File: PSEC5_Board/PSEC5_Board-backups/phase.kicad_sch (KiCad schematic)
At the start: 23 parts, among them U1 MC100LVEL40DWG, U4 OPA607QDBVRQ1, U7 AD4008BCPZ-RL7, Y1 ASE2-40.000MHZ-ET

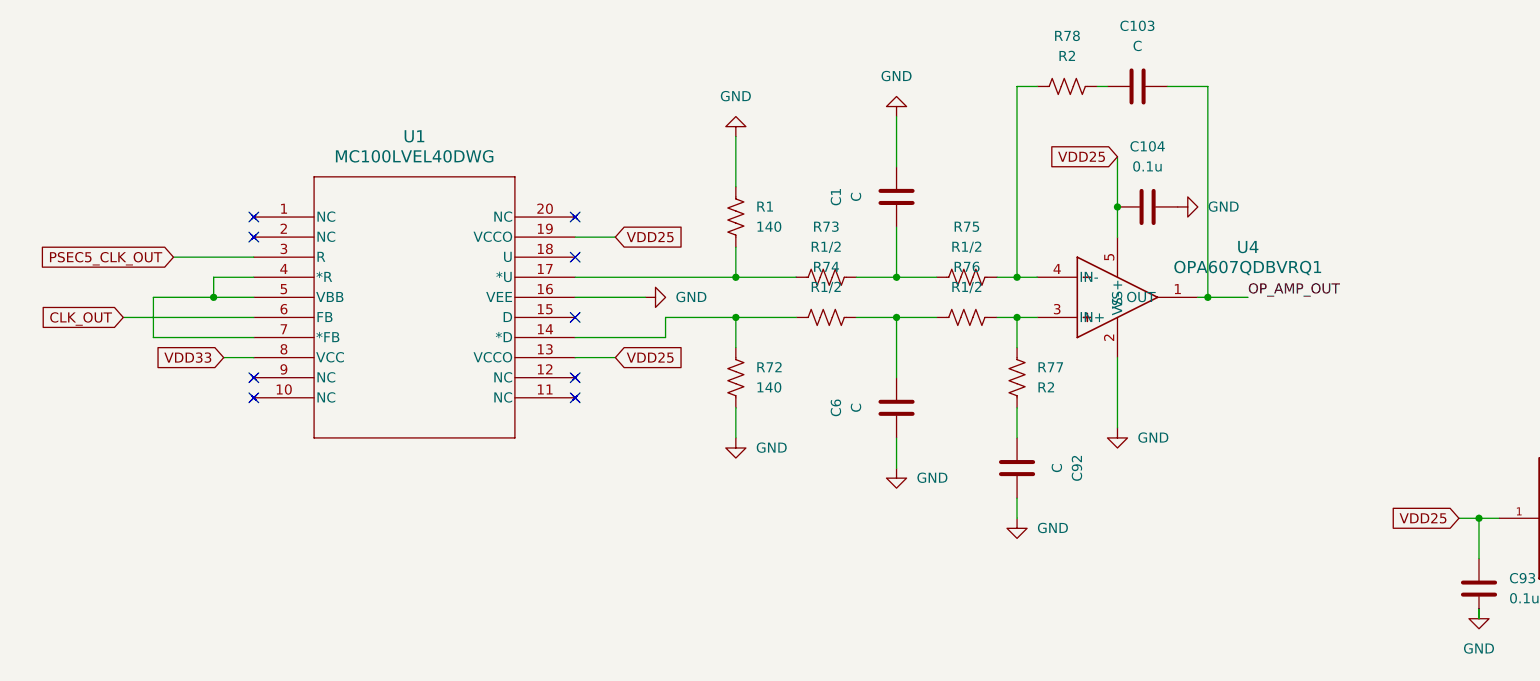
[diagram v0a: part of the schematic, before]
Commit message: DUT Review 1 Push
Cleared all ERC errors, Implemented Split plane, modified Phase detector, doubled up vias for power pads.
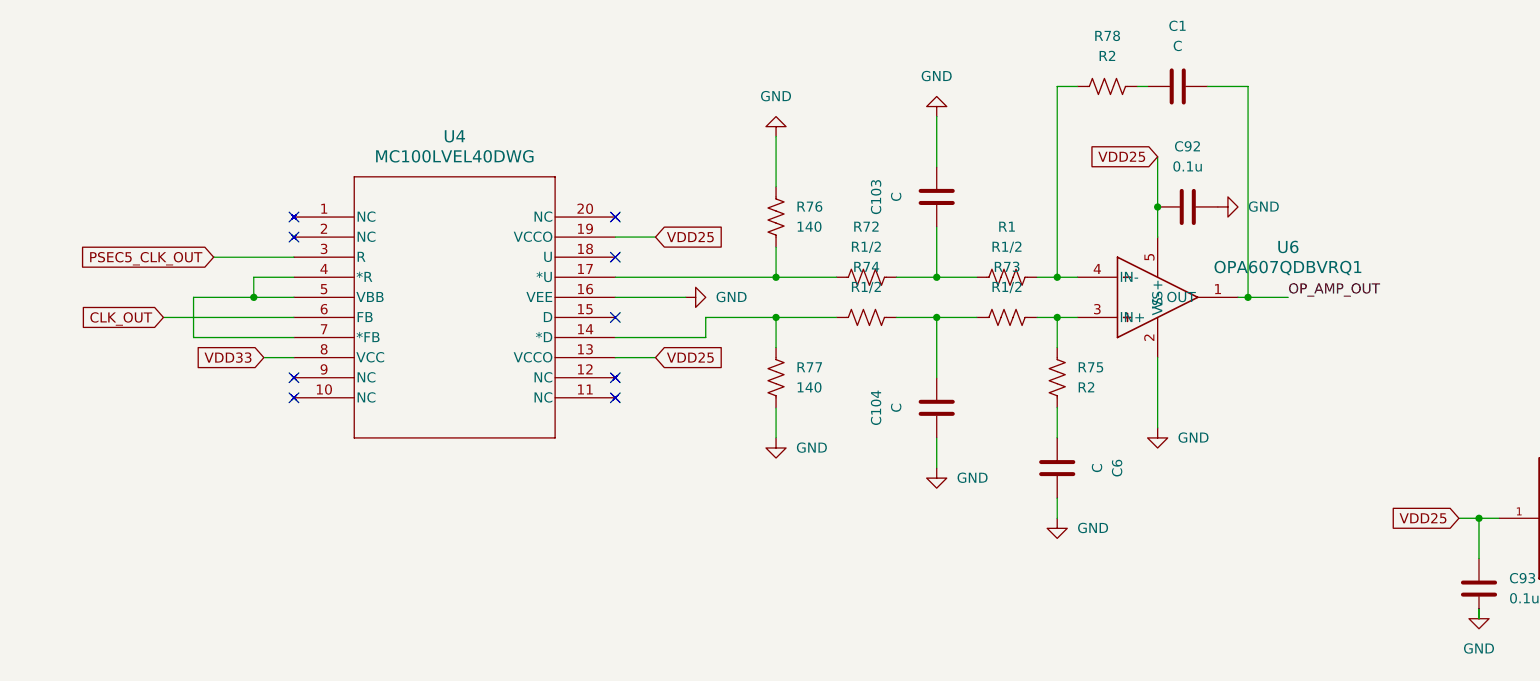
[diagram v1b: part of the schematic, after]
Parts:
- removed U1: MC100LVEL40DWG, MC100LVEL40DWG:SOP65P640X120-20N, symbol MC100LVEL40DWG_B:MC100LVEL40DWG
- removed U4: OPA607QDBVRQ1, footprints:DBV0005A-IPC_A, symbol 2024-09-19_16-57-49:OPA607QDBVRQ1
- added U4: MC100LVEL40DWG, MC100LVEL40DWG:SOP65P640X120-20N, symbol MC100LVEL40DWG_B:MC100LVEL40DWG
- added U6: OPA607QDBVRQ1, footprints:DBV0005A-IPC_A, symbol 2024-09-19_16-57-49:OPA607QDBVRQ1
- C104: value 0.1u -> C
- C92: value C -> 0.1u
- R1, R72: value 140 -> R1/2
- R75: value R1/2 -> R2
- R76: value R1/2 -> 140
- R77: value R2 -> 140
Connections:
- net CLK_OUT: now also U4.6 (FB)
- net GND: now also C103.1, C104.2, C6.1, R76.1, R77.1, U4.16 (VEE), U6.2 (VS-); no longer C1.1, C104.1, C6.2, R1.1, R72.1
- net OP_AMP_OUT: now also C1.1, U6.1 (OUT); no longer C103.1
- net PSEC5_CLK_OUT: now also U4.3 (R)
- net VDD25: now also C92.2, U4.13 (VCCO), U4.19 (VCCO), U6.5 (VS+); no longer C104.2
- net VDD33: now also U4.8 (VCC)
- net at C103.2: now also R1.2, R72.1; no longer R78.1
- net at R75.1: now also C6.2; no longer R78.2
- net at R73.1, R75.2: now also U6.3 (IN+); no longer C1.2
- net at R73.2: now also C104.1, R74.1; no longer R1.2
- net at R72.2: now also R76.2, U4.17 (*U); no longer R74.2
- net at R77.2: now also R74.2, U4.14 (*D); no longer R76.1
- new net: U4.4 (*R), U4.5 (VBB), U4.7 (*FB)
- new net: C1.2, R78.1
- new net: R1.1, R78.2, U6.4 (IN-)
